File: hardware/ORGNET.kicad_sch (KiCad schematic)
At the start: 41 parts, among them J1 Conn_02x08_Odd_Even, J3 Conn_01x03, U1 SN74LVC8T245, U2 SN74LVC8T245, U3 AP2112K-3.3, U4 RP2350A, U5 W25Q128JVP, U6 Raspberry Pi Radio Module 2, Y1 12M

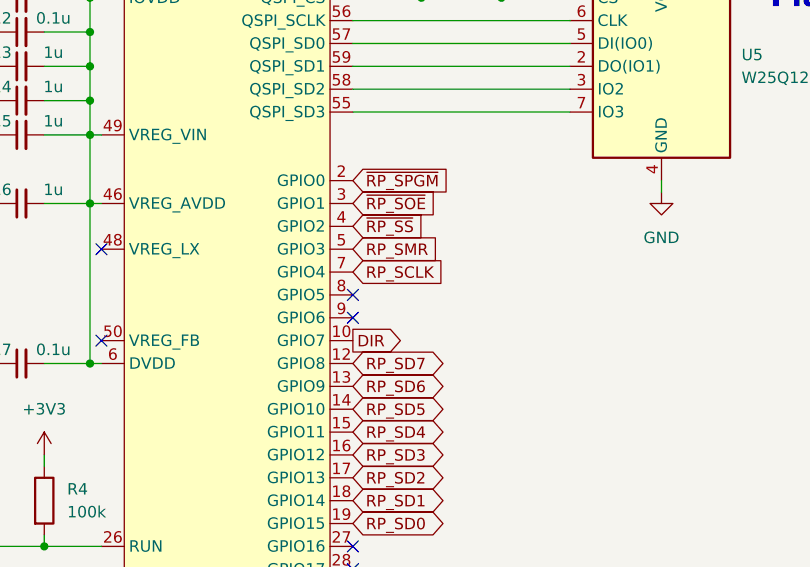
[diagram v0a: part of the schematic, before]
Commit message: Make a few minor changes to PCB layout and silkscreen
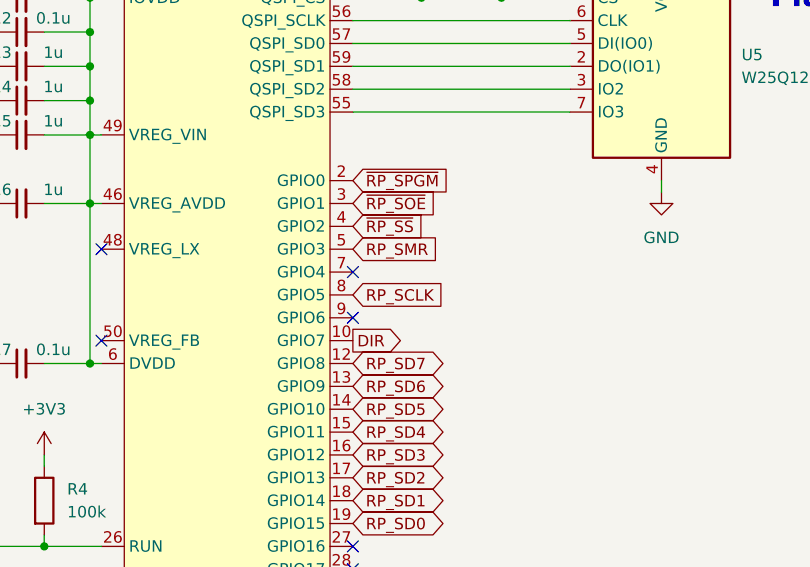
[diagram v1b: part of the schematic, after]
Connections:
- net RP_SCLK: now also U4.8 (GPIO5); no longer U4.7 (GPIO4)
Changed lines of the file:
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@@
+	)
+	(no_connect
+		(at 186.69 76.2)
 	)
 	(no_connect
@@
 	)
 	(no_connect
-		(at 186.69 76.2)
-	)
-	(no_connect
 		(at 158.75 106.68)
 	)
@@
 	)
 	(no_connect
-		(at 186.69 73.66)
+		(at 186.69 127)
 	)
 	(no_connect
-		(at 186.69 127)
+		(at 186.69 71.12)
 	)
 	(no_connect
@@
 		)
 	)
+	(global_label "RP_SCLK"
+		(shape input)
+		(at 186.69 73.66 0)
+		(fields_autoplaced yes)
+		(effects
+			(font
+				(size 1.27 1.27)
+			)
+			(justify left)
+		)
+		(property "Intersheetrefs" "${INTERSHEET_REFS}"
+			(at 197.9604 73.66 0)
+			(effects
+				(font
+					(size 1.27 1.27)
+				)
+				(justify left)
+				(hide yes)
+			)
+		)
+	)
 	(global_label "SMR"
 		(shape input)
@@
 				(hide yes)
 			)
-		)
-	)
-	(global_label "RP_SCLK"
-		(shape input)
-		(at 186.69 71.12 0)
-		(fields_autoplaced yes)
-		(effects
-			(font
-				(size 1.27 1.27)
-			)
-			(justify left)
-		)
-		(property "Intersheetrefs" "${INTERSHEET_REFS}"
-			(at 197.9604 71.12 0)
-			(effects
-				(font
-					(size 1.27 1.27)
-				)
-				(justify left)
-				(hide yes)
-			)

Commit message: Implement a few more minor PCB tweaks
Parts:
- C10, C11, C12, C9: value 0.1u -> 1u
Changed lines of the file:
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@@
 			)
 		)
-		(property "Value" "0.1u"
+		(property "Value" "1u"
 			(at 153.416 31.496 90)
 			(effects
@@
 			)
 		)
-		(property "Value" "0.1u"
+		(property "Value" "1u"
 			(at 153.416 35.306 90)
 			(effects
@@
 			)
 		)
-		(property "Value" "0.1u"
+		(property "Value" "1u"
 			(at 153.416 39.116 90)
 			(effects
@@
 			)
 		)
-		(property "Value" "0.1u"
+		(property "Value" "1u"
 			(at 153.416 42.926 90)
 			(effects

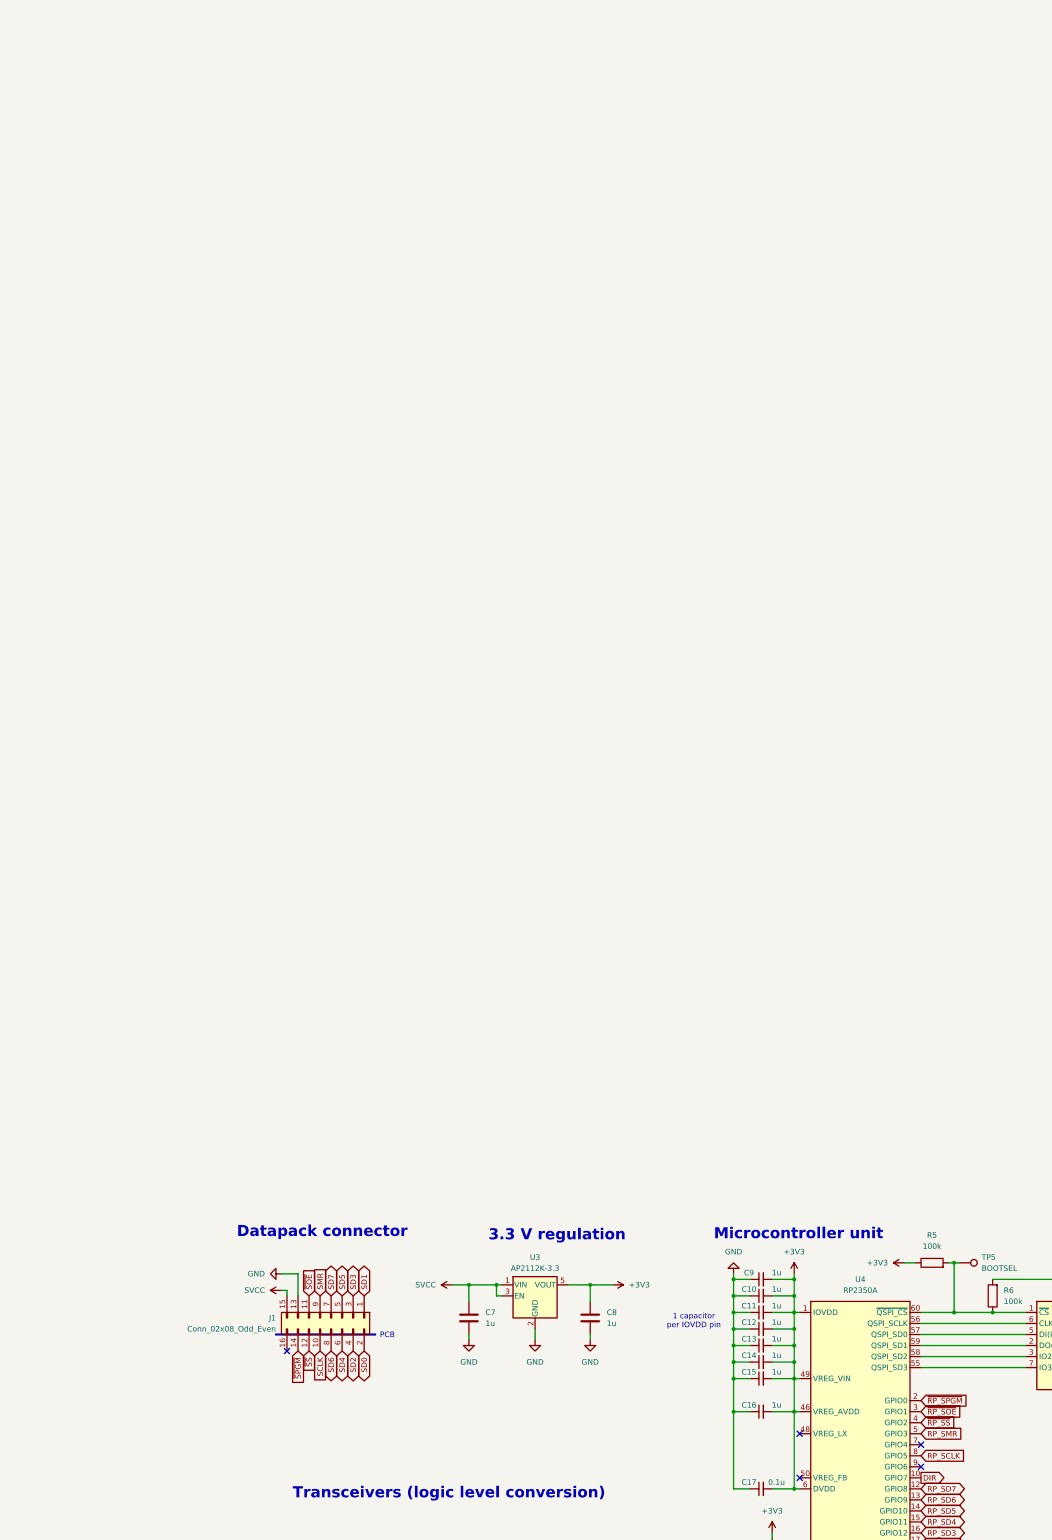
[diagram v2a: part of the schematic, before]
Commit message: Add notch and use 0406 resistors/capacitors
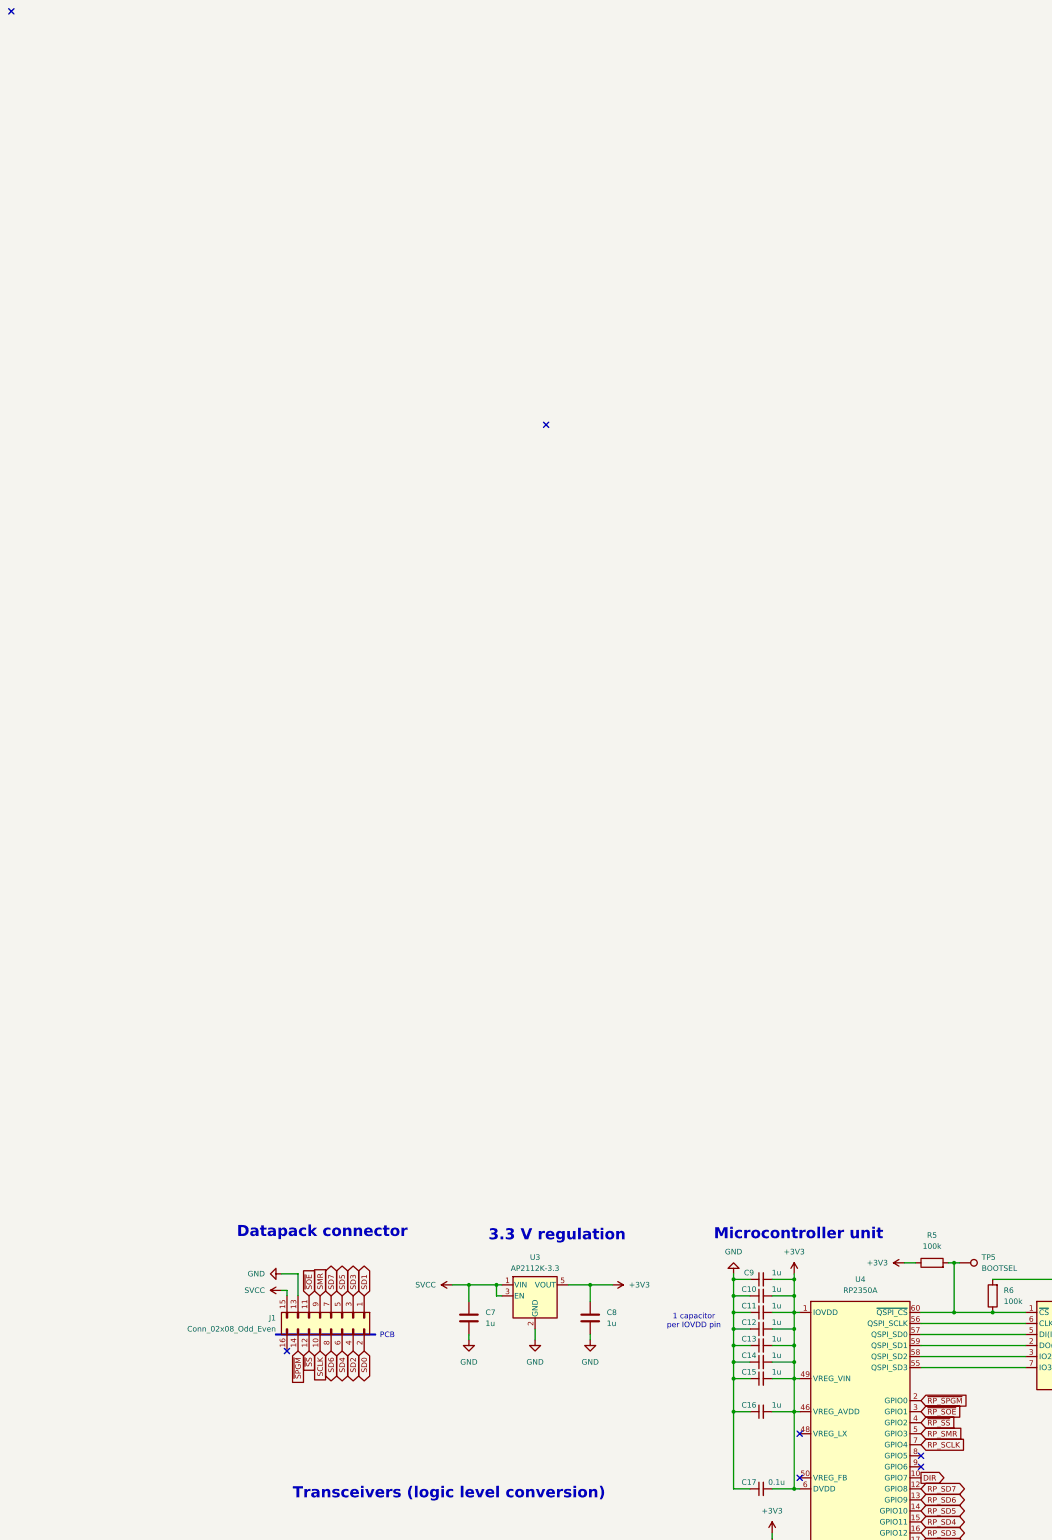
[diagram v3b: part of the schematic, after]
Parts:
- C1, C10, C11, C12, C13, C14, C15, C16, C17, C18, C19, C2, C3, C4, C5, C6, C7, C8, C9: footprint Capacitor_SMD:C_0201_0603Metric_Pad0.64x0.40mm_HandSolder -> Capacitor_SMD:C_0402_1005Metric_Pad0.74x0.62mm_HandSolder
- R1, R2, R3, R4, R5, R6, R7, R8: footprint Resistor_SMD:R_0201_0603Metric_Pad0.64x0.40mm_HandSolder -> Resistor_SMD:R_0402_1005Metric_Pad0.72x0.64mm_HandSolder
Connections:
- net RP_SCLK: now also U4.7 (GPIO4); no longer U4.8 (GPIO5)
- no-connect marks 23 -> 25
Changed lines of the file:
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@@
 	)
 	(no_connect
+		(at -22.86 -259.08)
+	)
+	(no_connect
 		(at 251.46 125.73)
 	)
@@
 	)
 	(no_connect
-		(at 186.69 71.12)
-	)
-	(no_connect
 		(at 186.69 114.3)
 	)
@@
 	)
 	(no_connect
+		(at 100.33 -163.83)
+	)
+	(no_connect
 		(at 186.69 109.22)
 	)
@@
 	)
 	(no_connect
+		(at 186.69 73.66)
+	)
+	(no_connect
 		(at 186.69 106.68)
 	)
@@
 		)
 	)
-	(global_label "RP_SCLK"
-		(shape input)
-		(at 186.69 73.66 0)
-		(fields_autoplaced yes)
-		(effects
-			(font
-				(size 1.27 1.27)
-			)
-			(justify left)
-		)
-		(property "Intersheetrefs" "${INTERSHEET_REFS}"
-			(at 197.9604 73.66 0)
-			(effects
-				(font
-					(size 1.27 1.27)
-				)
-				(justify left)
-				(hide yes)
-			)
-		)
-	)
 	(global_label "SMR"
 		(shape input)
@@
 		)
 	)
+	(global_label "RP_SCLK"
+		(shape input)
+		(at 186.69 71.12 0)
+		(fields_autoplaced yes)
+		(effects
+			(font
+				(size 1.27 1.27)
+			)
+			(justify left)
+		)
+		(property "Intersheetrefs" "${INTERSHEET_REFS}"
+			(at 197.9604 71.12 0)
+			(effects
+				(font
+					(size 1.27 1.27)
+				)
+				(justify left)
+				(hide yes)
+			)
+		)
+	)
 	(global_label "~{SOE}"
 		(shape input)
@@
 			)
 		)
-		(property "Footprint" "Capacitor_SMD:C_0201_0603Metric_Pad0.64x0.40mm_HandSolder"
+		(property "Footprint" "Capacitor_SMD:C_0402_1005Metric_Pad0.74x0.62mm_HandSolder"
 			(at 104.14 106.3752 0)
 			(effects
@@
 			)
 		)
-		(property "Footprint" "Capacitor_SMD:C_0201_0603Metric_Pad0.64x0.40mm_HandSolder"
+		(property "Footprint" "Capacitor_SMD:C_0402_1005Metric_Pad0.74x0.62mm_HandSolder"
 			(at 83.5152 45.72 0)
 			(effects
@@
 			)
 		)
-		(property "Footprint" "Capacitor_SMD:C_0201_0603Metric_Pad0.64x0.40mm_HandSolder"
+		(property "Footprint" "Capacitor_SMD:C_0402_1005Metric_Pad0.74x0.62mm_HandSolder"
 			(at 149.86 48.26 0)
 			(effects
@@
 			)
 		)
-		(property "Footprint" "Capacitor_SMD:C_0201_0603Metric_Pad0.64x0.40mm_HandSolder"
+		(property "Footprint" "Capacitor_SMD:C_0402_1005Metric_Pad0.74x0.62mm_HandSolder"
 			(at 53.34 121.6152 0)
 			(effects
@@
 			)
 		)
-		(property "Footprint" "Capacitor_SMD:C_0201_0603Metric_Pad0.64x0.40mm_HandSolder"
+		(property "Footprint" "Capacitor_SMD:C_0402_1005Metric_Pad0.74x0.62mm_HandSolder"
 			(at 137.16 129.54 0)
 			(effects
@@
 			)
 		)
-		(property "Footprint" "Capacitor_SMD:C_0201_0603Metric_Pad0.64x0.40mm_HandSolder"
+		(property "Footprint" "Capacitor_SMD:C_0402_1005Metric_Pad0.74x0.62mm_HandSolder"
 			(at 104.14 121.6152 0)
 			(effects
@@
 			)
 		)
-		(property "Footprint" "Capacitor_SMD:C_0201_0603Metric_Pad0.64x0.40mm_HandSolder"
+		(property "Footprint" "Capacitor_SMD:C_0402_1005Metric_Pad0.74x0.62mm_HandSolder"
 			(at 38.1 121.6152 0)
 			(effects
@@
 			)
 		)
-		(property "Footprint" "Capacitor_SMD:C_0201_0603Metric_Pad0.64x0.40mm_HandSolder"
+		(property "Footprint" "Capacitor_SMD:C_0402_1005Metric_Pad0.74x0.62mm_HandSolder"
 			(at 53.34 106.3752 0)
 			(effects
@@
 			)
 		)
-		(property "Footprint" "Capacitor_SMD:C_0201_0603Metric_Pad0.64x0.40mm_HandSolder"
+		(property "Footprint" "Capacitor_SMD:C_0402_1005Metric_Pad0.74x0.62mm_HandSolder"
 			(at 88.9 121.6152 0)
 			(effects
@@
 			)
 		)
-		(property "Footprint" "Capacitor_SMD:C_0201_0603Metric_Pad0.64x0.40mm_HandSolder"
+		(property "Footprint" "Capacitor_SMD:C_0402_1005Metric_Pad0.74x0.62mm_HandSolder"
 			(at 149.86 52.07 0)
 			(effects
@@
 			)
 		)
-		(property "Footprint" "Resistor_SMD:R_0201_0603Metric_Pad0.64x0.40mm_HandSolder"
+		(property "Footprint" "Resistor_SMD:R_0402_1005Metric_Pad0.72x0.64mm_HandSolder"
 			(at 84.582 180.34 90)
 			(effects
@@
 			)
 		)
-		(property "Footprint" "Capacitor_SMD:C_0201_0603Metric_Pad0.64x0.40mm_HandSolder"
+		(property "Footprint" "Capacitor_SMD:C_0402_1005Metric_Pad0.74x0.62mm_HandSolder"
 			(at 149.86 33.02 0)
 			(effects
@@
 			)
 		)
-		(property "Footprint" "Resistor_SMD:R_0201_0603Metric_Pad0.64x0.40mm_HandSolder"
+		(property "Footprint" "Resistor_SMD:R_0402_1005Metric_Pad0.72x0.64mm_HandSolder"
 			(at 73.152 180.34 90)
 			(effects
@@
 			)
 		)
-		(property "Footprint" "Capacitor_SMD:C_0201_0603Metric_Pad0.64x0.40mm_HandSolder"
+		(property "Footprint" "Capacitor_SMD:C_0402_1005Metric_Pad0.74x0.62mm_HandSolder"
 			(at 149.86 63.5 0)
 			(effects
@@
 			)
 		)
-		(property "Footprint" "Resistor_SMD:R_0201_0603Metric_Pad0.64x0.40mm_HandSolder"
+		(property "Footprint" "Resistor_SMD:R_0402_1005Metric_Pad0.72x0.64mm_HandSolder"
 			(at 204.978 36.83 90)
 			(effects
@@
 			)
 		)
-		(property "Footprint" "Capacitor_SMD:C_0201_0603Metric_Pad0.64x0.40mm_HandSolder"
+		(property "Footprint" "Capacitor_SMD:C_0402_1005Metric_Pad0.74x0.62mm_HandSolder"
 			(at 149.86 36.83 0)
 			(effects
@@
 			)
 		)
-		(property "Footprint" "Resistor_SMD:R_0201_0603Metric_Pad0.64x0.40mm_HandSolder"
+		(property "Footprint" "Resistor_SMD:R_0402_1005Metric_Pad0.72x0.64mm_HandSolder"
 			(at 27.432 180.34 90)
 			(effects
@@
 			)
 		)
-		(property "Footprint" "Resistor_SMD:R_0201_0603Metric_Pad0.64x0.40mm_HandSolder"
+		(property "Footprint" "Resistor_SMD:R_0402_1005Metric_Pad0.72x0.64mm_HandSolder"
 			(at 189.23 30.988 90)
 			(effects
@@
 			)
 		)
-		(property "Footprint" "Capacitor_SMD:C_0201_0603Metric_Pad0.64x0.40mm_HandSolder"
+		(property "Footprint" "Capacitor_SMD:C_0402_1005Metric_Pad0.74x0.62mm_HandSolder"
 			(at 149.86 40.64 0)
 			(effects
@@
 			)
 		)
-		(property "Footprint" "Capacitor_SMD:C_0201_0603Metric_Pad0.64x0.40mm_HandSolder"
+		(property "Footprint" "Capacitor_SMD:C_0402_1005Metric_Pad0.74x0.62mm_HandSolder"
 			(at 149.86 44.45 0)
 			(effects
@@
 			)
 		)
-		(property "Footprint" "Capacitor_SMD:C_0201_0603Metric_Pad0.64x0.40mm_HandSolder"
+		(property "Footprint" "Capacitor_SMD:C_0402_1005Metric_Pad0.74x0.62mm_HandSolder"
 			(at 111.4552 45.72 0)
 			(effects
@@
 			)
 		)
-		(property "Footprint" "Resistor_SMD:R_0201_0603Metric_Pad0.64x0.40mm_HandSolder"
+		(property "Footprint" "Resistor_SMD:R_0402_1005Metric_Pad0.72x0.64mm_HandSolder"
 			(at 251.46 116.332 90)
 			(effects
@@
 			)
 		)
-		(property "Footprint" "Resistor_SMD:R_0201_0603Metric_Pad0.64x0.40mm_HandSolder"
+		(property "Footprint" "Resistor_SMD:R_0402_1005Metric_Pad0.72x0.64mm_HandSolder"
 			(at 150.622 96.52 90)
 			(effects
@@
 			)
 		)
-		(property "Footprint" "Resistor_SMD:R_0201_0603Metric_Pad0.64x0.40mm_HandSolder"
+		(property "Footprint" "Resistor_SMD:R_0402_1005Metric_Pad0.72x0.64mm_HandSolder"
 			(at 269.748 134.62 90)
 			(effects
@@
 			)
 		)
-		(property "Footprint" "Capacitor_SMD:C_0201_0603Metric_Pad0.64x0.40mm_HandSolder"
+		(property "Footprint" "Capacitor_SMD:C_0402_1005Metric_Pad0.74x0.62mm_HandSolder"
 			(at 149.86 55.88 0)
 			(effects
@@
 			)
 		)
-		(property "Footprint" "Capacitor_SMD:C_0201_0603Metric_Pad0.64x0.40mm_HandSolder"
+		(property "Footprint" "Capacitor_SMD:C_0402_1005Metric_Pad0.74x0.62mm_HandSolder"
 			(at 137.16 121.92 0)
 			(effects
@@
 			)
 		)
-		(property "Footprint" "Capacitor_SMD:C_0201_0603Metric_Pad0.64x0.40mm_HandSolder"
+		(property "Footprint" "Capacitor_SMD:C_0402_1005Metric_Pad0.74x0.62mm_HandSolder"
 			(at 149.86 81.28 0)
 			(effects

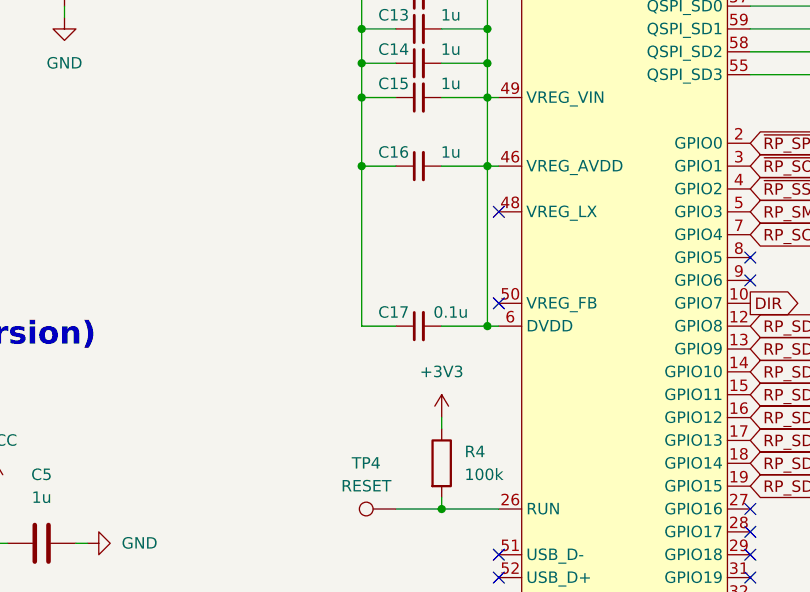
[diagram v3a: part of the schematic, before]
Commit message: Update schematic to fix MCU overheating
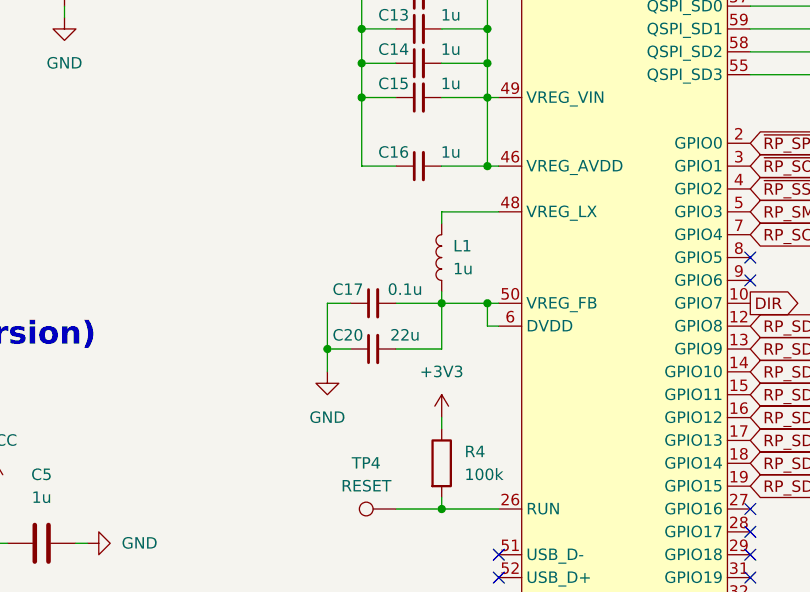
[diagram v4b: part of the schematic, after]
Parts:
- added C20: 22u, Capacitor_SMD:C_0402_1005Metric_Pad0.74x0.62mm_HandSolder, symbol Device:C_Small
- added L1: 1u, Inductor_SMD:L_1008_2520Metric_Pad1.43x2.20mm_HandSolder, symbol Device:L
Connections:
- net +3V3: no longer C17.2, U4.23 (DVDD), U4.39 (DVDD), U4.6 (DVDD)
- net GND: now also C20.1
- net at U4.48 (VREG_LX): now also L1.2
- net at U4.50 (VREG_FB): now also C17.2, U4.23 (DVDD), U4.39 (DVDD), U4.6 (DVDD), C20.2, L1.1
- no-connect marks 25 -> 23
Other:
- moved on the sheet: C17
